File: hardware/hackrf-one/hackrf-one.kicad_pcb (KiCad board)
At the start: 4 copper layers, 120 x 75 mm, 436 parts, among them J10 GND_CLIP, J11 Connector_USB_C_Receptacle_US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, J2 RF-SHIELD-FRAME, J3 RF-SHIELD-COVER, J4 MOUNTING_HOLE, J5 MOUNTING_HOLE, J6 MOUNTING_HOLE, J7 MOUNTING_HOLE, J8 MOUNTING_HOLE, J9 MOUNTING_HOLE, P1 1V8, P13 GPO1, P14 XCVR_CLKOUT, P15 INTR, P16 CLKIN, P17 GPO6, P18 OEB, P19 GPO3, P2 CLKOUT, P20 GPIO, P21 REF_IN, P22 I2S, P23 DBGEN, P24 TRST, P25 LPC_ISP, P26 LPC_JTAG, P27 MIXER_SDATA, P28 SD, P29 CPLD_JTAG, P3 GND, P30 BANK2_AUX, P31 MIXER_SCLK, P32 MIXER_ENX, P33 MIXER_RESETX, P34 MIX_BYPASS, P35 !MIX_BYPASS, P36 VAA, P37 SCL, P38 SDA, P39 SSP1_SCK, P4 ANTENNA, P40 SSP1_MOSI, P41 SSP1_MISO, P43 RX, P44 HP, P45 LP, P46 TX_MIX_BP, P47 RX_MIX_BP, P48 TX_AMP, P49 RX_AMP, P5 LEDS, P50 AMP_BYPASS, P51 !TX_AMP_PWR, P52 !RX_AMP_PWR, P53 CS_XCVR, P54 CS_AD, P55 TXENABLE, P56 RXENABLE, P57 XTAL2, P58 GCK1, P59 GCK2, P6 GPO4, P60 SGPIO_CLK, P61 DA0, P62 DA7, P63 DD0, P64 DD9, P65 DA4, P66 DD5, P67 RSSI, P68 SPIFI_CS, P69 VREGMODE, P7 GPO2, P70 EN_1V8, P72 GP_CLKIN, P73 P1_2, P74 P1_1, P75 GP_CLKIN, P76 GP_CLKIN, P77 GP_CLKIN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

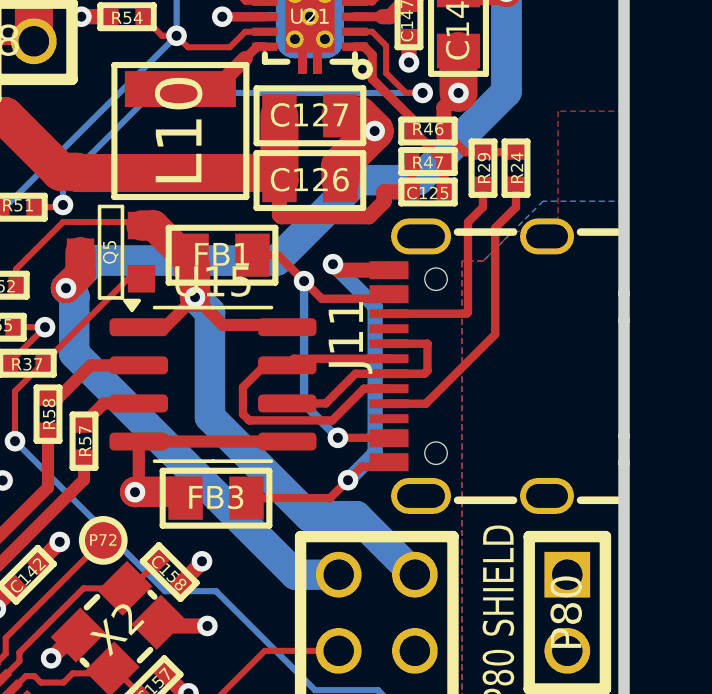
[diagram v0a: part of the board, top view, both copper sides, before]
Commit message: Made USB-C connector poke out 0.7mm
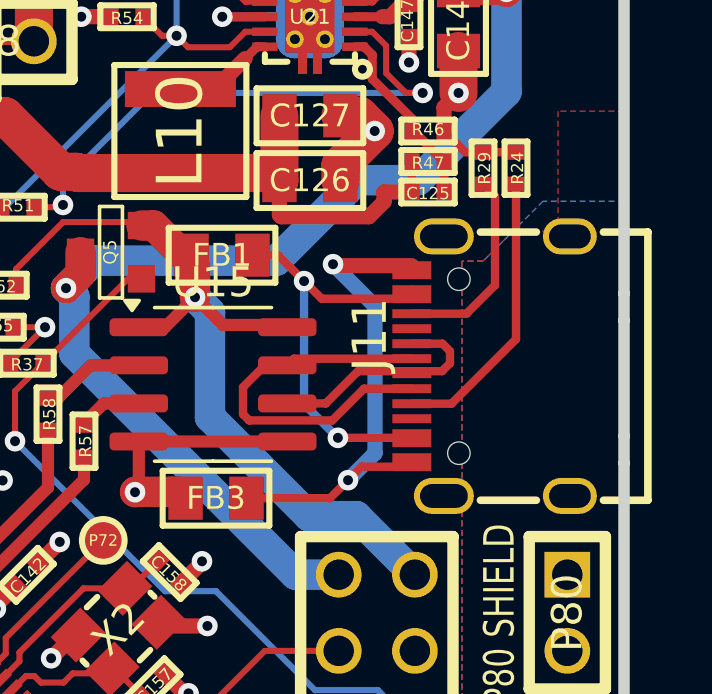
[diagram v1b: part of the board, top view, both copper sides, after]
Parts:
- moved J11 0.76 mm to (164.4, 105.9)
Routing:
- net Net-(J11-D--PadA7): track 11.5 -> 13.1 mm
- net Net-(FB3-Pad1): track 15.3 -> 16.7 mm
- net Net-(FB1-Pad1): track 13.2 -> 14.3 mm
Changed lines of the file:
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@@
 	(footprint "gsg-modules:USB-C_SMD-TYPE-C-31-M-12"
 		(layer "F.Cu")
-		(at 163.6226 105.8556 90)
+		(at 164.3841 105.8556 90)
 		(property "Reference" "J11"
 			(at -0.175 -4.03 90)
@@
 	)
 	(segment
-		(start 160.9886 103.6056)
-		(end 160.9886 103.3056)
+		(start 161.588145 108.243645)
+		(end 161.7501 108.4056)
 		(width 0.2794)
 		(layer "F.Cu")
@@
 	)
 	(segment
-		(start 159.284921 108.243645)
-		(end 160.826645 108.243645)
-		(width 0.2794)
-		(layer "F.Cu")
-		(net 382)
-	)
-	(segment
-		(start 160.9886 108.4056)
-		(end 160.9886 108.1056)
+		(start 161.4501 103.6056)
+		(end 161.7501 103.3056)
 		(width 0.2794)
 		(layer "F.Cu")
@@
 	)
 	(segment
-		(start 160.9886 103.6056)
-		(end 158.74331 103.6056)
+		(start 159.284921 108.243645)
+		(end 161.588145 108.243645)
 		(width 0.2794)
 		(layer "F.Cu")
@@
 	(segment
 		(start 157.29331 102.1556)
-		(end 156.4386 102.1556)
+		(end 158.74331 103.6056)
 		(width 0.2794)
 		(layer "F.Cu")
@@
 	)
 	(segment
-		(start 158.74331 103.6056)
+		(start 156.4386 102.1556)
 		(end 157.29331 102.1556)
 		(width 0.2794)
@@
 	)
 	(segment
-		(start 160.826645 108.243645)
-		(end 160.9886 108.4056)
+		(start 158.74331 103.6056)
+		(end 161.4501 103.6056)
 		(width 0.2794)
 		(layer "F.Cu")
@@
 	)
 	(segment
-		(start 164.529 101.2492)
-		(end 164.529 104.7946)
-		(width 0.2794)
-		(layer "F.Cu")
-		(net 383)
-	)
-	(segment
-		(start 165.2226 100.5556)
-		(end 164.529 101.2492)
-		(width 0.2794)
-		(layer "F.Cu")
-		(net 383)
-	)
-	(segment
-		(start 162.218 107.1056)
-		(end 160.9886 107.1056)
+		(start 165.2226 99.789)
+		(end 165.2226 104.9556)
 		(width 0.2794)
 		(layer "F.Cu")
@@
 	)
 	(segment
-		(start 164.529 104.7946)
-		(end 162.218 107.1056)
+		(start 165.2226 104.9556)
+		(end 163.0726 107.1056)
 		(width 0.2794)
 		(layer "F.Cu")
@@
 	)
 	(segment
-		(start 165.2226 99.789)
-		(end 165.2226 100.5556)
+		(start 163.0726 107.1056)
+		(end 161.7501 107.1056)
 		(width 0.2794)
 		(layer "F.Cu")
@@
 	)
 	(segment
-		(start 164.1226 100.5556)
-		(end 163.6226 101.0556)
-		(width 0.2794)
-		(layer "F.Cu")
-		(net 384)
-	)
-	(segment
-		(start 163.6226 101.0556)
-		(end 163.6226 104.0556)
-		(width 0.2794)
-		(layer "F.Cu")
-		(net 384)
-	)
-	(segment
 		(start 163.5726 104.1056)
-		(end 160.9886 104.1056)
+		(end 161.7501 104.1056)
 		(width 0.2794)
 		(layer "F.Cu")
@@
 	)
 	(segment
-		(start 163.6226 104.0556)
-		(end 163.5726 104.1056)
+		(start 164.5226 100.189)
+		(end 164.5226 103.1556)
 		(width 0.2794)
 		(layer "F.Cu")
@@
 	(segment
 		(start 164.1226 99.789)
-		(end 164.1226 100.5556)
+		(end 164.5226 100.189)
 		(width 0.2794)
 		(layer "F.Cu")
@@
 	)
 	(segment
-		(start 157.819 105.6056)
-		(end 157.5976 105.827)
+		(start 164.5226 103.1556)
+		(end 163.5726 104.1056)
 		(width 0.2794)
 		(layer "F.Cu")
-		(net 385)
+		(net 384)
 	)
 	(segment
-		(start 160.9886 106.6056)
-		(end 160.1552 106.6056)
+		(start 161.7501 105.6056)
+		(end 157.819 105.6056)
 		(width 0.2794)
 		(layer "F.Cu")
@@
 	)
 	(segment
-		(start 156.3307 107.6637)
-		(end 156.1226 107.4556)
+		(start 156.8512 105.827)
+		(end 157.5976 105.827)
 		(width 0.2794)
 		(layer "F.Cu")
@@
 	)
 	(segment
-		(start 156.8512 105.827)
+		(start 157.819 105.6056)
 		(end 157.5976 105.827)
 		(width 0.2794)
@@
 	)
 	(segment
-		(start 160.9886 105.6056)
-		(end 157.819 105.6056)
+		(start 160.1552 106.6056)
+		(end 159.0971 107.6637)
 		(width 0.2794)
 		(layer "F.Cu")
@@
 	)
 	(segment
-		(start 160.1552 106.6056)
-		(end 159.0971 107.6637)
+		(start 156.3307 107.6637)
+		(end 156.1226 107.4556)
 		(width 0.2794)
 		(layer "F.Cu")
@@
 	)
 	(segment
-		(start 162.1726 106.1056)
-		(end 160.9886 106.1056)
+		(start 161.7501 106.6056)
+		(end 160.1552 106.6056)
 		(width 0.2794)
 		(layer "F.Cu")
-		(net 386)
+		(net 385)
 	)
 	(segment
-		(start 160.9886 105.1056)
-		(end 162.2726 105.1056)
+		(start 163.0226 105.3556)
+		(end 163.0226 105.7556)
 		(width 0.2794)
 		(layer "F.Cu")
@@
 	)
 	(segment
-		(start 159.8726 106.1056)
-		(end 160.9886 106.1056)
+		(start 161.7501 105.1056)
+		(end 162.7726 105.1056)
 		(width 0.2794)
 		(layer "F.Cu")
@@
 	)
 	(segment
-		(start 162.2726 105.1056)
-		(end 162.2726 106.0056)
+		(start 159.9559 106.0223)
+		(end 158.8812 107.097)
 		(width 0.2794)
 		(layer "F.Cu")
@@
 	)
 	(segment
-		(start 157.5976 107.097)
-		(end 158.8812 107.097)
+		(start 163.0226 105.7556)
+		(end 162.7559 106.0223)
 		(width 0.2794)
 		(layer "F.Cu")
@@
 	)
 	(segment
-		(start 162.2726 106.0056)
-		(end 162.1726 106.1056)
+		(start 162.7559 106.0223)
+		(end 159.9559 106.0223)
 		(width 0.2794)
 		(layer "F.Cu")
@@
 	(segment
 		(start 158.8812 107.097)
-		(end 159.8726 106.1056)
+		(end 157.5976 107.097)
 		(width 0.2794)
 		(layer "F.Cu")
@@
 	)
 	(segment
-		(start 159.1226 102.4556)
-		(end 159.3226 102.6556)
-		(width 0.508)
+		(start 162.7726 105.1056)
+		(end 163.0226 105.3556)
+		(width 0.2794)
 		(layer "F.Cu")
-		(net 389)
+		(net 386)
 	)
 	(segment
-		(start 159.3226 102.6556)
-		(end 160.8386 102.6556)
+		(start 159.1726 102.5056)
+		(end 159.1226 102.4556)
 		(width 0.508)
 		(layer "F.Cu")
@@
 	)
 	(segment
-		(start 159.0226 110.2556)
-		(end 159.6226 109.6556)
-		(width 0.2794)
+		(start 161.7501 102.5056)
+		(end 159.1726 102.5056)
+		(width 0.508)
 		(layer "F.Cu")
 		(net 389)
 	)
 	(segment
-		(start 160.0726 109.2056)
+		(start 159.0226 110.2556)
 		(end 159.6226 109.6556)
 		(width 0.2794)
@@
 	)
 	(segment
-		(start 160.8386 102.6556)
-		(end 160.9886 102.5056)
-		(width 0.3048)
+		(start 161.7501 109.2056)
+		(end 160.0726 109.2056)
+		(width 0.2794)
 		(layer "F.Cu")
 		(net 389)
 	)
 	(segment
-		(start 160.9886 109.2056)
-		(end 160.0726 109.2056)
+		(start 156.2386 110.2556)
+		(end 159.0226 110.2556)
 		(width 0.2794)
 		(layer "F.Cu")
@@
 	)
 	(segment
-		(start 156.2386 110.2556)
-		(end 159.0226 110.2556)
+		(start 160.0726 109.2056)
+		(end 159.6226 109.6556)
 		(width 0.2794)
 		(layer "F.Cu")

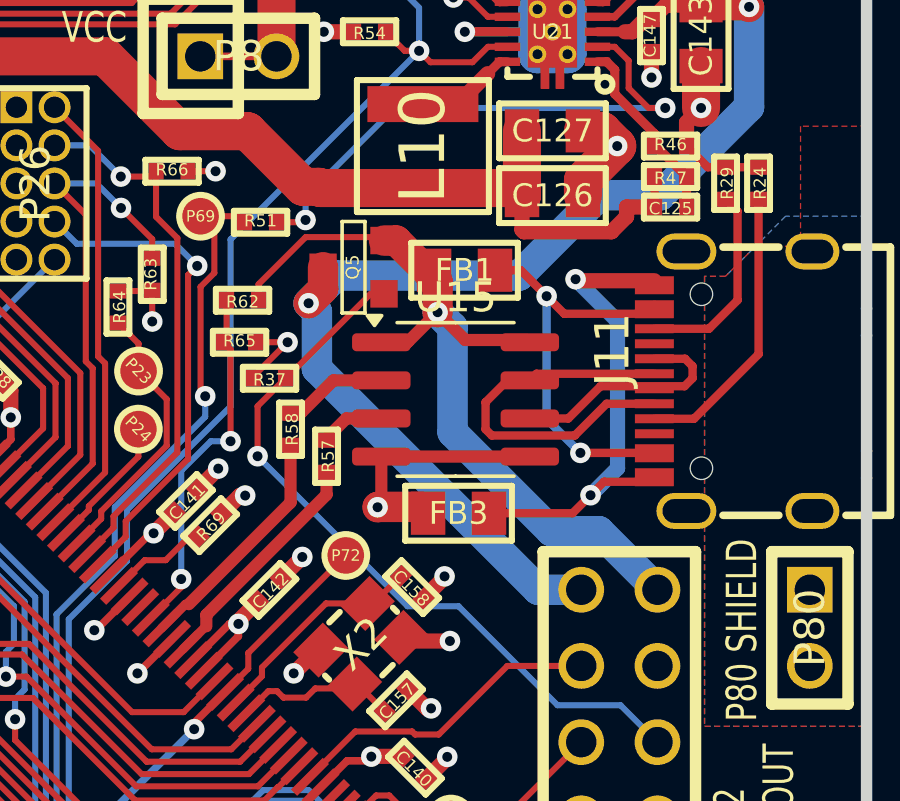
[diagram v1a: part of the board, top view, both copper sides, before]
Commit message: Change USB protection to ECMF02-4CMX8
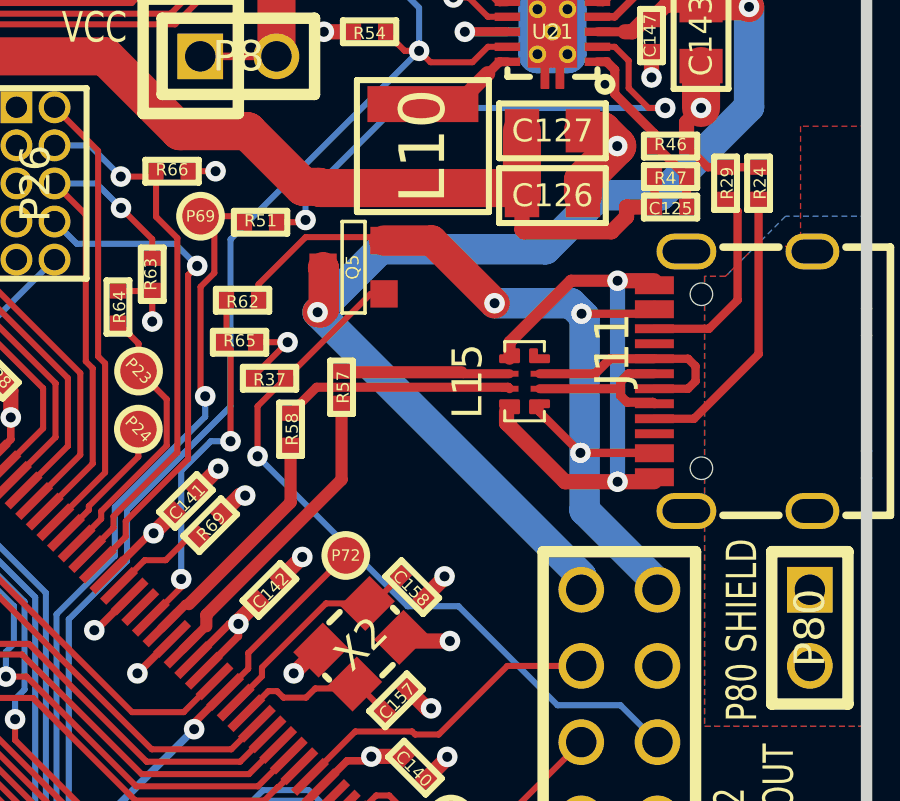
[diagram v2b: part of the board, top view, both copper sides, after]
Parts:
- removed FB1, FB3: FILTER, hackrf:GSG-0805
- removed U15: USB6B1, Package_SO:SOIC-8_3.9x4.9mm_P1.27mm
- added L15: ECMF02-4CMX8, gsg-modules:QFN-8_L2.5-W1.2-P0.50-BL, F.Cu at (157.4, 105.9)
- moved R57 2.35 mm to (151.3, 106.1)
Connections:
- J11 pad A1: Net-(FB3-Pad1) -> GND
- J11 pad A12: Net-(FB3-Pad1) -> GND
- J11 pad A4: Net-(FB1-Pad1) -> /mcu/usb/power/VBUS
- J11 pad A9: Net-(FB1-Pad1) -> /mcu/usb/power/VBUS
- J11 pad B1: Net-(FB3-Pad1) -> GND
- J11 pad B12: Net-(FB3-Pad1) -> GND
- J11 pad B4: Net-(FB1-Pad1) -> /mcu/usb/power/VBUS
- J11 pad B9: Net-(FB1-Pad1) -> /mcu/usb/power/VBUS
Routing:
- net Net-(FB3-Pad1): track 16.7 -> 0.00 mm, vias 2 -> 0
- net Net-(FB1-Pad1): track 14.3 -> 0.00 mm, vias 2 -> 0
- net GND: track 596.7 -> 605.6 mm, vias 219 -> 220
- net Net-(J11-D--PadA7): track 13.1 -> 5.66 mm
- net Net-(L15-D--Pad7): track 3.48 -> 7.68 mm
- net Net-(L15-D+-Pad6): track 2.16 -> 5.52 mm
- net /mcu/usb/power/VBUS: track 28.9 -> 31.8 mm, vias 1 -> 3
- net /mcu/usb/power/DP: track 7.93 -> 10.4 mm
- net /mcu/usb/power/VIN: track 43.0 -> 41.9 mm
